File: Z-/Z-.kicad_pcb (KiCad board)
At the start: 4 copper layers, 98 x 98 mm, 144 parts, among them J1 200528-0100, J2 U.FL, J3 U.FL, J4 200528-0100, J5 Conn_01x02, K1 IM02DGR, Q1 NX3008NBKS, Q10 NX3008NBKS, Q11 IRLML2803, Q12 MBT2222ADW1T1, Q13 IRLML2803, Q14 NX3008NBKS, Q15 IRF7404, Q16 MBT2222ADW1T1, Q17 IRF7404, Q18 IRLML2803, Q19 IRF7404, Q2 NX3008NBKS, Q3 MBT2222ADW1T1, Q4 MBT2222ADW1T1, Q5 NX3008NBKS, Q6 NX3008NBKS, Q7 MBT2222ADW1T1, Q8 MBT2222ADW1T1, Q9 MMBT2222AT, U1 OPT4003DNPRQ1, U2 LTC4316xDD, U3 ADM1176-1ARMZ-R7, U4 NCV891330PD50R2G, U5 DRV8830DRC

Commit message: Z- Solar Panel files upload
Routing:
- net VDRIVE: track 32.0 -> 30.6 mm
- net SDA: track 97.2 -> 96.6 mm
- net SCL: track 90.8 -> 90.2 mm
- net Net-(D1-A): track 7.13 -> 6.58 mm

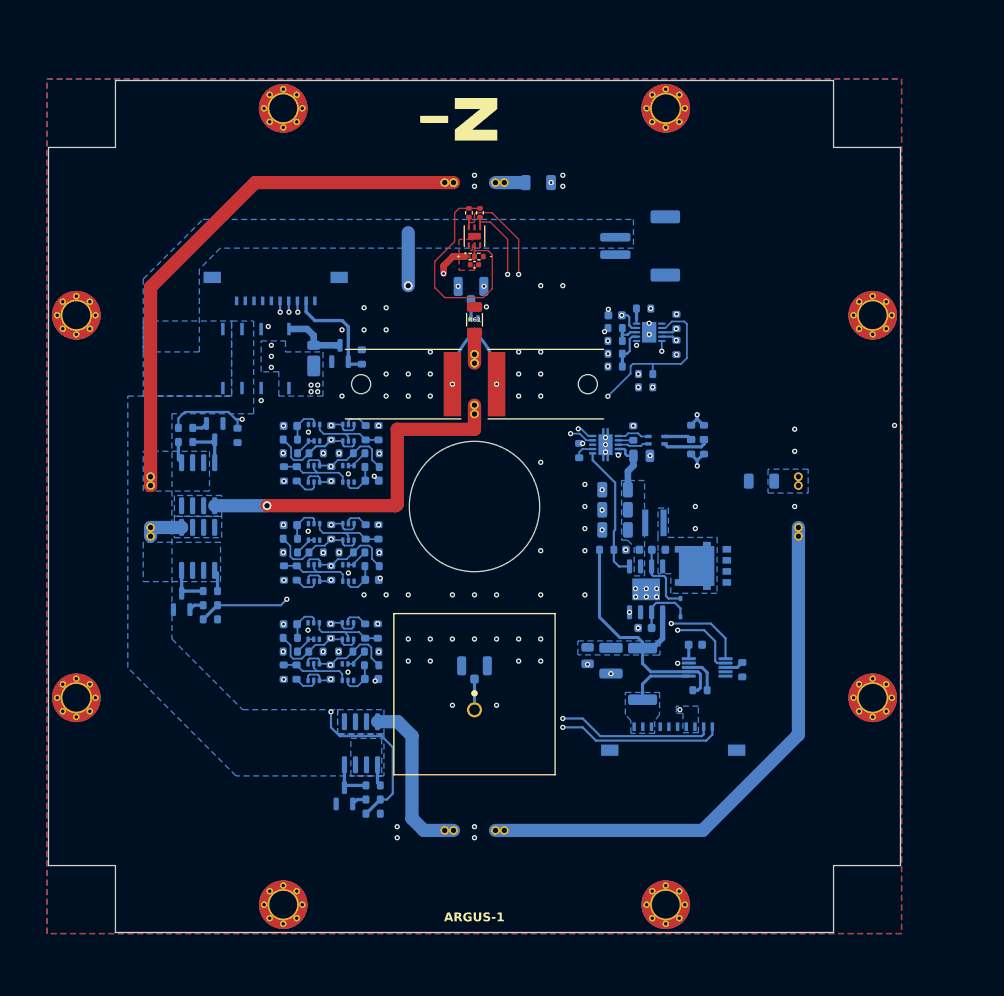
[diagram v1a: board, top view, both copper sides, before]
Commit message: Added i2c expander for burnwires, reformatted i2c protection, swapped to drv8235
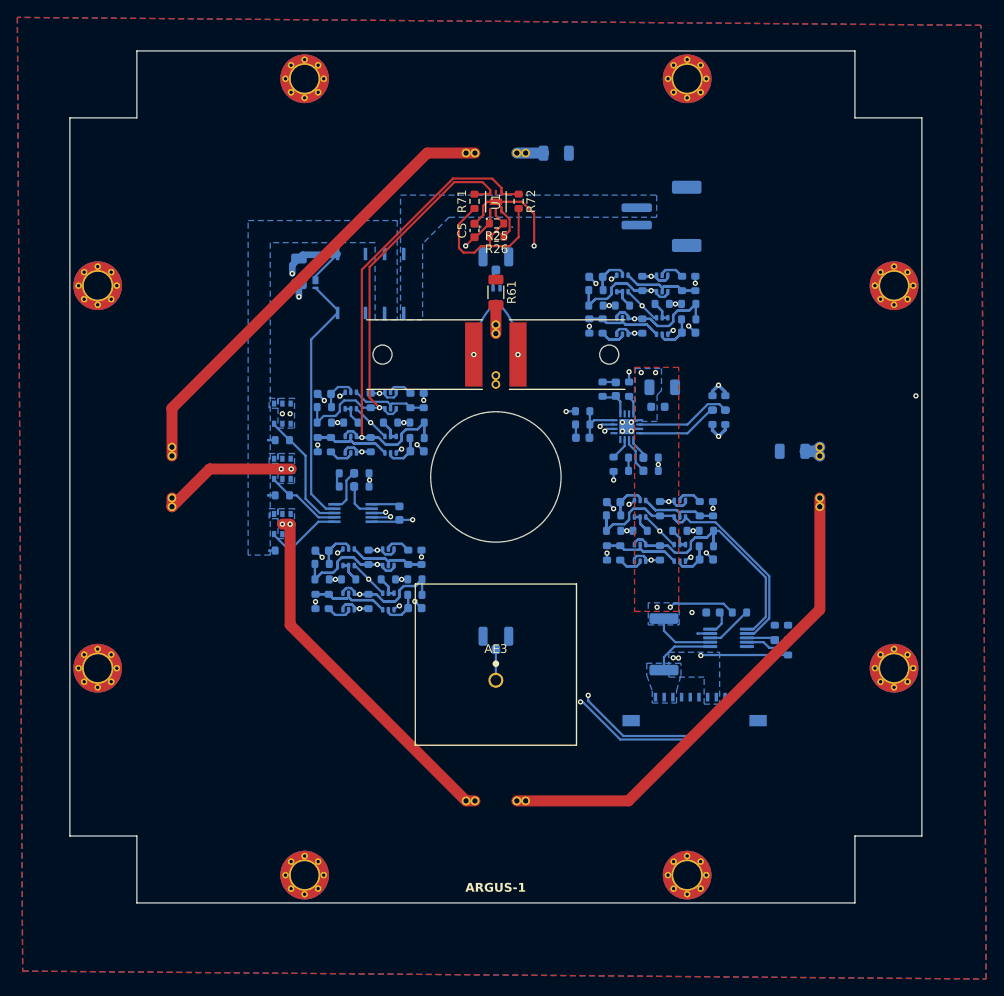
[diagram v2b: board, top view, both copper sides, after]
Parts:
- removed C17: 0.1uF, Capacitor_SMD:C_0603_1608Metric
- removed C18: 10nF, Capacitor_SMD:C_0603_1608Metric
- removed D2: NRVB440MFS, SolarPanels:NRVB440MFSWFT1G
- removed D3: DFLS130L, Diode_SMD:D_PowerDI-123
- removed FL1: SRF2012, SolarPanels:SRF2012
- removed G***: LOGO, LOGO
- removed J4: 200528-0100, Connector_FFC-FPC:Molex_200528-0100_1x10-1MP_P1.00mm_Horizontal
- removed L1: XGL3520-222, SolarPanels:XGL3520
- removed R15, R16, R35, R36, R47, R48: DNI (0R), Resistor_SMD:R_0603_1608Metric
- removed Ref**: Val**, custom-footprints:ypanel
- removed U5: DRV8830DRC, Package_SON:VSON-10-1EP_3x3mm_P0.5mm_EP1.65x2.4mm
- added R73: 10K, Resistor_SMD:R_0603_1608Metric, B.Cu at (175.3, 73.4)
- added R74: 10K, Resistor_SMD:R_0603_1608Metric, B.Cu at (163.8, 75.9)
- added R75: 200K, Resistor_SMD:R_0603_1608Metric, B.Cu at (163.8, 74.2)
- added R76: 680R, Resistor_SMD:R_0603_1608Metric, B.Cu at (166.6, 104.4)
- added R77: 100K, Resistor_SMD:R_0603_1608Metric, B.Cu at (173.5, 101.9)
- added R78: DNI (0R), Resistor_SMD:R_0603_1608Metric, B.Cu at (171.2, 104.4)
- added R79: 10K, Resistor_SMD:R_0603_1608Metric, B.Cu at (165.1, 104.4)
- added R82: 10K, Resistor_SMD:R_0603_1608Metric, B.Cu at (176.5, 101.9)
- added R83: 200K, Resistor_SMD:R_0603_1608Metric, B.Cu at (176.5, 103.6)
- added R84: 680R, Resistor_SMD:R_0603_1608Metric, B.Cu at (175.8, 99.3)
- added R85: 100K, Resistor_SMD:R_0603_1608Metric, B.Cu at (168.9, 101.9)
- added R86: DNI (0R), Resistor_SMD:R_0603_1608Metric, B.Cu at (171.2, 99.3)
- added R87: 10K, Resistor_SMD:R_0603_1608Metric, B.Cu at (177.3, 99.3)
- added R88: 10K, Resistor_SMD:R_0603_1608Metric, B.Cu at (165.9, 101.9)
- added R89: 200K, Resistor_SMD:R_0603_1608Metric, B.Cu at (165.9, 100.1)
- C10: value 0.1uF -> 10uF; footprint Capacitor_SMD:C_0603_1608Metric -> Capacitor_SMD:C_1206_3216Metric
- C11, C12: value 0.1uF -> 10nF
- C13: value 10uF -> 0.1uF; footprint Capacitor_SMD:C_1206_3216Metric -> Capacitor_SMD:C_0603_1608Metric
- C14, C15: value 10uF -> 10nF; footprint Capacitor_SMD:C_1206_3216Metric -> Capacitor_SMD:C_0603_1608Metric
- C16: value 10nF -> 10uF; footprint Capacitor_SMD:C_0603_1608Metric -> Capacitor_SMD:C_1206_3216Metric
- C5: footprint Capacitor_SMD:C_0402_1005Metric -> Capacitor_SMD:C_0603_1608Metric
- C7: value 4.7uF -> 0.1uF; footprint Capacitor_SMD:C_1210_3225Metric -> Capacitor_SMD:C_0603_1608Metric
- C8: value 0.1uF -> 1nF; footprint Capacitor_SMD:C_0805_2012Metric -> Capacitor_SMD:C_0603_1608Metric
- C9: value 1uF -> 0.1uF; footprint Capacitor_SMD:C_0805_2012Metric -> Capacitor_SMD:C_0603_1608Metric
- D1: value BAS16HT1G -> PTVS5V0Z1USK; footprint Diode_SMD:D_SOD-323 -> Diode_SMD:Nexperia_DSN1608-2_1.6x0.8mm
- K1: value IM02DGR -> IM11DGR
- Q10, Q14, Q2, Q6: value NX3008NBKS -> MBT2222ADW1T1
- Q11, Q13: value IRLML2803 -> NX3008NBKS; footprint Package_TO_SOT_SMD:SOT-23 -> Package_TO_SOT_SMD:SOT-363_SC-70-6
- Q15, Q17, Q19: value IRF7404 -> IRFTS9342PBF; footprint Package_SO:SOIC-8_3.9x4.9mm_P1.27mm -> Package_SO:TSOP-6_1.65x3.05mm_P0.95mm
- Q16, Q3, Q7: value MBT2222ADW1T1 -> NX3008NBKS
- Q18: value IRLML2803 -> MBT2222ADW1T1; footprint Package_TO_SOT_SMD:SOT-23 -> Package_TO_SOT_SMD:SOT-363_SC-70-6
- Q9: value MMBT2222AT -> NX3008NBKS; footprint Package_TO_SOT_SMD:SOT-23 -> Package_TO_SOT_SMD:SOT-363_SC-70-6
- R12, R37, R39, R49, R56, R62: value 10K -> 0R
- R14, R40: value 100K -> 10K
- R18, R45: value 10K -> 200K
- R19, R33: value 10K -> 680R
- R20, R34: value 200K -> 100K
- R21, R29: value 10K -> DNI (0R)
- R22: value 200K -> 10K
- R23: value 680R -> 10K
- R24: value 680R -> 200K
- R25, R26, R71, R72: footprint Resistor_SMD:R_0402_1005Metric -> Resistor_SMD:R_0603_1608Metric
- R27: value 100K -> 680R
- R3, R50: value 680R -> 100K
- R38: value 680R -> DNI (0R)
- R41, R51, R59: value 4.7K -> 0R
- R46: value 200K -> 680R
- R5, R52: value 100K -> DNI (0R)
- R63: value 10K -> 10k
- R64: value 10K -> TBD
- R65: value ? -> TBD
- R66: value ? -> 560R
- R67: value ? -> 0R
- R68: value ? -> 680R
- R69: value 0R (DNI) -> 100K
- R70: value 0R (DNI) -> DNI (0R)
- U2: value LTC4316xDD -> PCA9633DP2; footprint Package_DFN_QFN:DFN-10-1EP_3x3mm_P0.5mm_EP1.65x2.38mm -> SolarPanels:SOT552-1_NXP
- U4: value NCV891330PD50R2G -> DRV8235RTER; footprint Package_SO:SOIC-8-1EP_3.9x4.9mm_P1.27mm_EP2.514x3.2mm -> SolarPanels:WQFN16_RTE_TEX
- moved R59 73.8 mm to (185.9, 115.3), turned to -90 degrees
- moved R56 65.8 mm to (184.4, 113.5)
- moved Q11 62.5 mm to (166.9, 73.4)
- moved Q12 60.0 mm to (171.4, 73.4), turned to -90 degrees
- moved R58 58.7 mm to (174.5, 77.5), turned to 180 degrees
- moved R57 58.6 mm to (174.5, 75.8), turned to 0 degrees
- moved D1 56.2 mm to (131.6, 73.3)
- moved R52 55.2 mm to (169.2, 78.3), turned to -90 degrees
- moved Q18 54.2 mm to (173.5, 99.3)
- moved R39 53.5 mm to (170.2, 95.0)
- moved R49 52.0 mm to (170.2, 93.4)
- moved R41 51.3 mm to (168.4, 95.0)
- moved R50 50.8 mm to (171.4, 75.8), turned to 180 degrees
- moved Q10 50.8 mm to (166.9, 78.3), turned to 90 degrees
- moved R51 49.6 mm to (168.4, 93.4)
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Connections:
- C10 pad 1: GND -> VDRIVE
- C10 pad 2: Net-(D1-A) -> GND
- C11 pad 1: Net-(D1-K) -> Net-(Q9B-G1)
- C11 pad 2: /I2C Devices/SW -> GND
- C12 pad 1: GND -> Net-(Q11B-G1)
- C12 pad 2: +5V -> GND
- C13 pad 1: GND -> 3.3V
- C13 pad 2: +5V -> GND
- C14 pad 1: GND -> Net-(Q13B-G1)
- C14 pad 2: +5V -> GND
- C15 pad 1: GND -> Net-(Q16B-G1)
- C15 pad 2: +5V -> GND
- C16 pad 1: Net-(Q10B-G1) -> 3.3V
- C2 pad 1: Net-(Q2B-G1) -> Net-(Q3B-G1)
- C4 pad 1: Net-(Q6B-G1) -> Net-(Q7B-G1)
- C7 pad 1: GND -> /I2C Devices/VREF
- C7 pad 2: VDRIVE -> GND
- C8 pad 1: +5V -> /I2C Devices/IPROPI
- C9 pad 1: GND -> VDRIVE
- C9 pad 2: VDRIVE -> GND
- D1 pad 1: Net-(D1-K) -> 3.3V
- D1 pad 2: Net-(D1-A) -> BURN_RELAY_A
- K1 pad 1: VBATT -> 3.3V
- K1 pad 8: Net-(D3-A) -> BURN_RELAY_A
- Q10 pad 1: GND -> SCL
- Q10 pad 2: Net-(Q10A-G2) -> Net-(Q10A-B1)
- Q10 pad 3: Net-(Q10A-G2) -> SCL
- Q10 pad 4: GND -> SCL_M
- Q10 pad 5: Net-(Q10B-G1) -> Net-(Q10B-B2)
- Q10 pad 6: Net-(Q10A-D1) -> SCL_M
- Q11 pad 1: Net-(Q11-G) -> GND
- Q11 pad 2: GND -> Net-(Q11A-G2)
- Q11 pad 3: Net-(Q11-D) -> Net-(Q11A-G2)
- Q12 pad 1: SCL -> SDA
- Q12 pad 3: SCL -> SDA
- Q12 pad 4: SCL_CPWR -> SDA_M
- Q12 pad 5: Net-(Q10A-D1) -> Net-(Q11A-D1)
- Q12 pad 6: SCL_CPWR -> SDA_M
- Q13 pad 1: Net-(Q13-G) -> GND
- Q13 pad 2: GND -> Net-(Q13A-G2)
- Q13 pad 3: Net-(Q13-D) -> Net-(Q13A-G2)
- Q14 pad 1: GND -> SCL
- Q14 pad 2: Net-(Q14A-G2) -> Net-(Q14A-B1)
- Q14 pad 3: Net-(Q14A-G2) -> SCL
- Q14 pad 4: GND -> SCL_CPWR
- Q14 pad 5: Net-(Q14B-G1) -> Net-(Q13A-D1)
- Q14 pad 6: Net-(Q14A-D1) -> SCL_CPWR
- Q15 pad 1: /Burn Wires/VBURN_A_IN -> /Burn Wires/VBURN1
- Q15 pad 2: /Burn Wires/VBURN_A_IN -> /Burn Wires/VBURN1
- Q15 pad 3: /Burn Wires/VBURN_A_IN -> BURN_EN1
- Q15 pad 4: Net-(Q11-D) -> /Burn Wires/VBURN_A_IN
- Q16 pad 1: SDA -> GND
- Q16 pad 2: Net-(Q16A-B1) -> Net-(Q16A-G2)
- Q16 pad 3: SDA -> Net-(Q16A-G2)
- Q16 pad 4: SDA_CPWR -> GND
- Q16 pad 5: Net-(Q14A-D1) -> Net-(Q16B-G1)
- Q16 pad 6: SDA_CPWR -> Net-(Q16A-D1)
- Q17 pad 1: /Burn Wires/VBURN_A_IN -> /Burn Wires/VBURN2
- Q17 pad 2: /Burn Wires/VBURN_A_IN -> /Burn Wires/VBURN2
- Q17 pad 3: /Burn Wires/VBURN_A_IN -> BURN_EN2
- Q17 pad 4: Net-(Q13-D) -> /Burn Wires/VBURN_A_IN
- Q18 pad 1: Net-(Q18-G) -> SDA
- Q18 pad 2: GND -> Net-(Q18A-B1)
- Q18 pad 3: Net-(Q18-D) -> SDA
- Q19 pad 1: /Burn Wires/VBURN_A_IN -> /Burn Wires/VBURN3
- Q19 pad 2: /Burn Wires/VBURN_A_IN -> /Burn Wires/VBURN3
- Q19 pad 3: /Burn Wires/VBURN_A_IN -> BURN_EN3
- Q19 pad 4: Net-(Q18-D) -> /Burn Wires/VBURN_A_IN
- Q2 pad 1: GND -> SCL
- Q2 pad 2: Net-(Q2A-G2) -> Net-(Q2A-B1)
- Q2 pad 3: Net-(Q2A-G2) -> SCL
- Q2 pad 4: GND -> SCL_LS
- Q2 pad 5: Net-(Q2B-G1) -> Net-(Q1A-D1)
- Q2 pad 6: Net-(Q2A-D1) -> SCL_LS
- Q3 pad 1: SCL -> GND
- Q3 pad 2: Net-(Q3A-B1) -> Net-(Q3A-G2)
- Q3 pad 3: SCL -> Net-(Q3A-G2)
- Q3 pad 4: SCL_LS -> GND
- Q3 pad 5: Net-(Q1A-D1) -> Net-(Q3B-G1)
- Q3 pad 6: SCL_LS -> Net-(Q3A-D1)
- Q4 pad 1: SCL -> SDA
- Q4 pad 3: SCL -> SDA
- Q4 pad 4: SCL_M -> SDA_LS
- Q4 pad 5: Net-(Q2A-D1) -> Net-(Q3A-D1)
- Q4 pad 6: SCL_M -> SDA_LS
- Q6 pad 1: GND -> SCL
- Q6 pad 2: Net-(Q6A-G2) -> Net-(Q6A-B1)
- Q6 pad 3: Net-(Q6A-G2) -> SCL
- Q6 pad 4: GND -> SCL_IO
- Q6 pad 5: Net-(Q6B-G1) -> Net-(Q5A-D1)
- Q6 pad 6: Net-(Q6A-D1) -> SCL_IO
- Q7 pad 1: SDA -> GND
- Q7 pad 2: Net-(Q7A-B1) -> Net-(Q7A-G2)
- Q7 pad 3: SDA -> Net-(Q7A-G2)
- Q7 pad 4: SDA_LS -> GND
- Q7 pad 5: Net-(Q5A-D1) -> Net-(Q7B-G1)
- Q7 pad 6: SDA_LS -> Net-(Q7A-D1)
- Q8 pad 4: SDA_M -> SDA_IO
- Q8 pad 5: Net-(Q6A-D1) -> Net-(Q7A-D1)
- Q8 pad 6: SDA_M -> SDA_IO
- Q9 pad 1: BURN_RELAY_A -> GND
- Q9 pad 2: GND -> Net-(Q9A-G2)
- Q9 pad 3: Net-(D3-A) -> Net-(Q9A-G2)
- R1 pad 1: Net-(Q3A-B1) -> Net-(Q2A-B1)
- R10 pad 1: GND -> /I2C Devices/A0_CPWR
- R10 pad 2: Net-(U3-A0) -> 3.3V
- R11 pad 1: GND -> /I2C Devices/A0_IO
- R11 pad 2: Net-(U5-A0) -> 3.3V
- R12 pad 1: M_FAULT -> GND
- R12 pad 2: VDRIVE -> /I2C Devices/A0_IO
- R13 pad 1: GND -> /I2C Devices/A1_IO
- R13 pad 2: Net-(U5-ISENSE) -> 3.3V
- R14 pad 2: Net-(Q2A-G2) -> Net-(Q1A-D1)
- R17 pad 2: Net-(Q1A-D1) -> SCL_LS
- R18 pad 1: 3.3V -> SCL_LS
- R18 pad 2: Net-(Q2A-D1) -> Net-(Q1B-G1)
- R19 pad 1: 3.3V -> Net-(Q4A-B1)
- R19 pad 2: SCL_LS -> Net-(Q3A-D1)
- R20 pad 1: SCL_LS -> 3.3V
- R20 pad 2: Net-(Q1B-G1) -> Net-(Q3A-G2)
- R21 pad 1: 3.3V -> SDA_LS
- R21 pad 2: SCL_M -> SDA
- R22 pad 1: SCL_M -> 3.3V
- R22 pad 2: Net-(Q2B-G1) -> Net-(Q3A-D1)
- R23 pad 1: Net-(Q7A-B1) -> 3.3V
- R23 pad 2: Net-(Q5A-D1) -> SDA_LS
- R24 pad 1: Net-(Q8A-B1) -> SDA_LS
- R24 pad 2: Net-(Q6A-D1) -> Net-(Q3B-G1)
- R27 pad 1: 3.3V -> Net-(Q6A-B1)
- R27 pad 2: Net-(Q5A-G2) -> Net-(Q5A-D1)
- R28 pad 2: Net-(Q6A-G2) -> Net-(Q5A-G2)
- R29 pad 1: 3.3V -> SCL_IO
- R29 pad 2: Net-(Q5A-D1) -> SCL
- R3 pad 1: Net-(Q4A-B1) -> 3.3V
- R3 pad 2: Net-(Q2A-D1) -> Net-(Q1A-G2)
- R30 pad 2: Net-(Q6A-D1) -> Net-(Q5A-D1)
- R31 pad 2: SDA_LS -> SCL_IO
- R32 pad 1: SDA_LS -> SCL_IO
- R33 pad 1: 3.3V -> Net-(Q8A-B1)
- R33 pad 2: SDA_M -> Net-(Q7A-D1)
- R34 pad 1: SDA_M -> 3.3V
- R34 pad 2: Net-(Q6B-G1) -> Net-(Q7A-G2)
- R37 pad 1: BURN_RELAY_A -> GND
- R37 pad 2: GND -> /I2C Devices/A1_IO
- R38 pad 1: Net-(Q12A-B1) -> SDA_IO
- R38 pad 2: Net-(Q10A-D1) -> SDA
- R39 pad 1: BURN_EN1 -> /I2C Devices/A0_COIL
- R39 pad 2: GND -> 3.3V
- R40 pad 2: Net-(Q10A-G2) -> Net-(Q7A-D1)
- R41 pad 1: Net-(Q11-G) -> GND
- R41 pad 2: BURN_EN1 -> /I2C Devices/A0_COIL
- R42 pad 2: Net-(Q10A-D1) -> SDA_IO
- R43 pad 1: Net-(Q11-D) -> BURN_EN1
- R45 pad 1: 3.3V -> SDA_IO
- R45 pad 2: SCL_CPWR -> Net-(Q7B-G1)
- R46 pad 1: SCL_CPWR -> Net-(Q10A-B1)
- R46 pad 2: Net-(Q10B-G1) -> Net-(Q10B-B2)
- R49 pad 1: BURN_EN2 -> /I2C Devices/A1_COIL
- R49 pad 2: GND -> 3.3V
- R5 pad 1: 3.3V -> SCL_LS
- R5 pad 2: Net-(Q1A-G2) -> SCL
- R50 pad 1: Net-(Q16A-B1) -> 3.3V
- R50 pad 2: Net-(Q14A-D1) -> Net-(Q9A-G2)
- R51 pad 1: Net-(Q13-G) -> GND
- R51 pad 2: BURN_EN2 -> /I2C Devices/A1_COIL
- R52 pad 1: 3.3V -> SCL_M
- R52 pad 2: Net-(Q14A-G2) -> SCL
- R53 pad 1: Net-(Q13-D) -> BURN_EN2
- R54 pad 2: Net-(Q14A-D1) -> Net-(Q10B-B2)
- R56 pad 1: BURN_EN3 -> GND
- R56 pad 2: GND -> /I2C Devices/A0_CPWR
- R57 pad 2: SDA_CPWR -> SCL_M
- R58 pad 1: SDA_CPWR -> SCL_M
- R58 pad 2: Net-(Q14B-G1) -> Net-(Q9B-G1)
- R59 pad 1: Net-(Q18-G) -> /I2C Devices/A1_CPWR
- R59 pad 2: BURN_EN3 -> 3.3V
- R60 pad 1: Net-(Q18-D) -> BURN_EN3
- R62 pad 1: Net-(U2-ENABLE) -> GND
- R62 pad 2: 3.3V -> /I2C Devices/A1_CPWR
- R63 pad 1: /I2C Devices/SDAOUT -> 3.3V
- R63 pad 2: 3.3V -> Net-(U4-NFAULT)
- R64 pad 1: /I2C Devices/SCLOUT -> 3.3V
- R64 pad 2: 3.3V -> /I2C Devices/VREF
- R65 pad 1: GND -> /I2C Devices/VREF
- R65 pad 2: Net-(U2-XORL) -> GND
- R66 pad 1: Net-(U2-XORL) -> /I2C Devices/IPROPI
- R66 pad 2: 3.3V -> GND
- R67 pad 1: GND -> Net-(U4-NSLEEP)
- R67 pad 2: Net-(U2-XORH) -> 3.3V
- R68 pad 1: Net-(U2-XORH) -> Net-(Q12A-B1)
- R68 pad 2: 3.3V -> Net-(Q11A-D1)
- R69 pad 1: SCL_LS -> 3.3V
- R69 pad 2: /I2C Devices/SCLOUT -> Net-(Q11A-G2)
- R70 pad 1: SDA_LS -> SDA_M
- R70 pad 2: /I2C Devices/SDAOUT -> SDA
- R71 pad 2: /I2C Devices/SDAOUT -> SDA_LS
- R72 pad 1: /I2C Devices/SCLOUT -> SCL_LS
- U1 pad 4: /I2C Devices/SCLOUT -> SCL_LS
- U1 pad 6: /I2C Devices/SDAOUT -> SDA_LS
- U2 pad 1: GND -> BURN_EN2
- U2 pad 10: SCL_LS -> 3.3V
- U2 pad 2: Net-(U2-XORH) -> BURN_EN1
- U2 pad 3: Net-(U2-XORL) -> BURN_EN3
- U2 pad 4: 3.3V -> BURN_RELAY_A
- U2 pad 5: Net-(U2-ENABLE) -> /I2C Devices/A0_IO
- U2 pad 6: unconnected-(U2-READY-Pad6) -> GND
- U2 pad 7: SDA_LS -> /I2C Devices/A1_IO
- U2 pad 8: /I2C Devices/SDAOUT -> SCL_IO
- U2 pad 9: /I2C Devices/SCLOUT -> SDA_IO
- U3 pad 8: Net-(U3-A0) -> /I2C Devices/A0_CPWR
- U3 pad 9: GND -> /I2C Devices/A1_CPWR
- U4 pad 1: VDRIVE -> /I2C Devices/IPROPI
- U4 pad 2: Net-(D1-A) -> unconnected-(U4-RSVD-Pad2)
- U4 pad 4: GND -> Net-(U4-NFAULT)
- U4 pad 5: M_FAULT -> VDRIVE
- U4 pad 6: +5V -> COIL_P
- U4 pad 7: Net-(D1-K) -> GND
- U4 pad 8: /I2C Devices/SW -> COIL_N
- U4 pad 9: GND -> /I2C Devices/A1_COIL
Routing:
- net GND: track 0.00 -> 65.1 mm, vias 107 -> 27
- net SDA: track 96.6 -> 161.1 mm, vias 4 -> 5
- net SCL: track 90.2 -> 154.7 mm, vias 4 -> 5
- net BURN_EN2: track 71.3 -> 9.15 mm, vias 2 -> 0
- net 3.3V: track 113.9 -> 64.6 mm, vias 26 -> 27
- net /I2C Devices/SDAOUT: track 47.3 -> 0.00 mm, vias 3 -> 0
- net /I2C Devices/SCLOUT: track 42.9 -> 0.00 mm, vias 3 -> 0
- net SCL_IO: track 0.00 -> 39.4 mm, vias 0 -> 2
- net BURN_EN1: track 45.4 -> 8.83 mm, vias 2 -> 0
- net SDA_IO: track 0.00 -> 35.4 mm, vias 0 -> 2
- net VBATT: track 27.7 -> 0.00 mm, vias 8 -> 0
- net /Burn Wires/VBURN2: track 19.5 -> 42.1 mm, vias 0 -> 2
- net SCL_CPWR: track 62.7 -> 42.6 mm, vias 2 -> 0
- net Net-(Q10B-B2): track 0.00 -> 19.5 mm
- net Net-(Q11A-D1): track 0.00 -> 18.1 mm
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- added copper zone on F.Cu, net VDRIVE
- removed copper zone on B.Cu, net +5V
- removed copper zone on B.Cu, net /I2C Devices/SW
- removed copper zone on F.Cu, net 3.3V
- removed copper zone on In1.Cu, net GND
- removed copper zone on B.Cu, net Net-(JP5-Pad2)
- removed copper zone on In1.Cu, net VBATT
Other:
- board text added: "ARGUS-1 Cubesat Carnegie Mellon University Z- Solar Panel v2"
- board text removed: "ALUN"
- board text removed: "ARGUS-1 Cubesat Carnegie Mellon University Z- Solar Panel v1"
- board text removed: "BURN WIRE 1"
- board text removed: "BURN WIRE 2"
- board text removed: "BURN WIRE 3"
- board text removed: "BURNWIRE 1"
- board text removed: "BURNWIRE 2"
- board text removed: "BURNWIRE 3"
- board text removed: "BURN_EN1"
- board text removed: "BURN_EN2"
- board text removed: "BURN_EN3"
- board text removed: "BURN_EN4"
- board text removed: "COIL DRIVER"
- board text removed: "COIL PWR MONITOR"
- board text removed: "GPS ANT"
- board text removed: "I2C ADDR TRANSLATOR"
- board text removed: "I2C BUS PROTECTION"
- board text removed: "MAINBOARD"
- board text removed: "POWER RELAY A"
- board text removed: "REGULATOR BUCK 5V"
- board text removed: "RELAY_A"
- board text removed: "UHF ANT"

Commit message: Moved burnwire around and added switch to coil driver
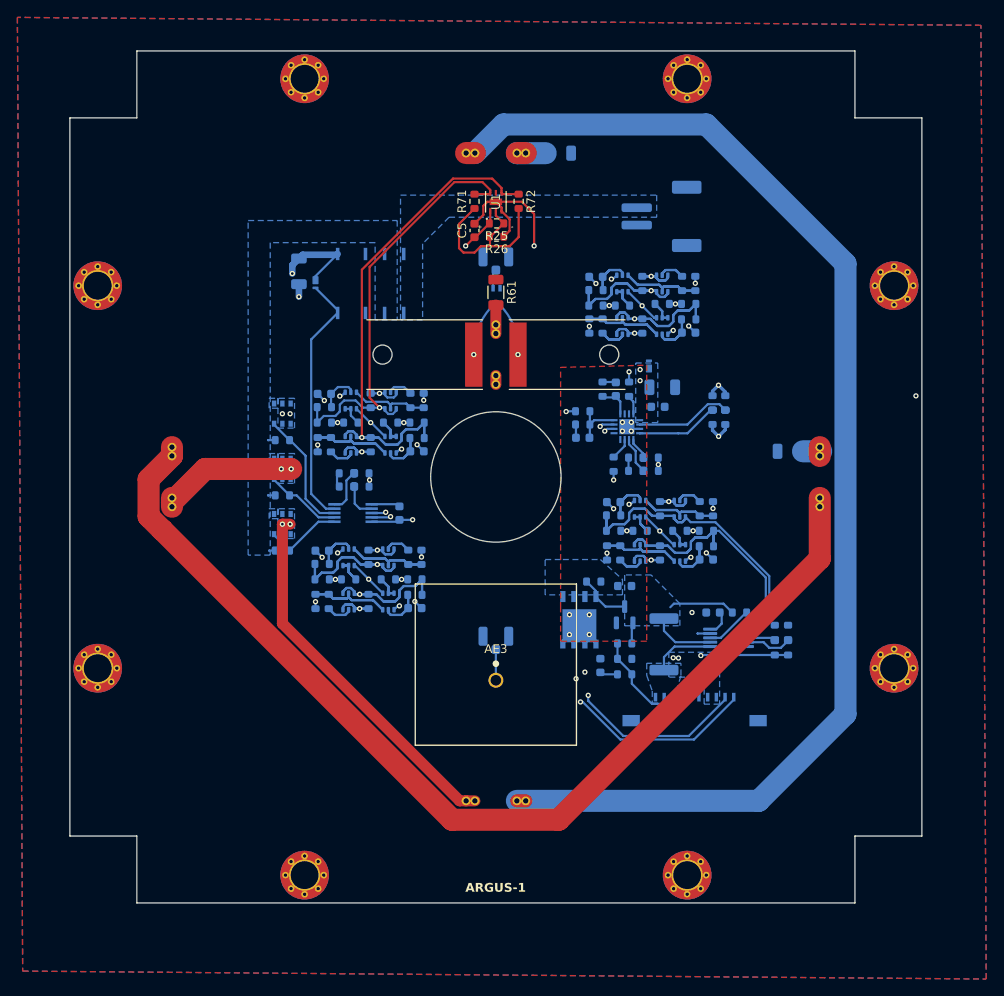
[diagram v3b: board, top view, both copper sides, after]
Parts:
- added D2: GREEN, LED_SMD:LED_0603_1608Metric, B.Cu at (164.3, 117.3)
- added D3: 10V, Diode_SMD:Nexperia_DSN1608-2_1.6x0.8mm, B.Cu at (169.9, 82.9)
- added F1: 500mA, Fuse:Fuse_0603_1608Metric, B.Cu at (167.1, 108.2)
- added Q20: IRLML2803, Package_TO_SOT_SMD:SOT-23, B.Cu at (167.1, 111.5)
- added Q21: SIRA99DP-T1-GE3, Package_SO:PowerPAK_SO-8_Single, B.Cu at (161.9, 112.1)
- added R15: 2.7k, Resistor_SMD:R_0603_1608Metric, B.Cu at (167.1, 118.4)
- added R16: 10k, Resistor_SMD:R_0603_1608Metric, B.Cu at (167.1, 116.6)
- added R35: 4k7, Resistor_SMD:R_0603_1608Metric, B.Cu at (167.1, 114.8)
- added R36: 10k, Resistor_SMD:R_0603_1608Metric, B.Cu at (163.6, 107.7)
- AE1, AE2: footprint SolarPanels:Antenna Mount -> Argus-Miscellaneous:Antenna Mount
- AE3: footprint SolarPanels:ANT_CGGBP.18.4.A.02_TAL -> Argus-Miscellaneous:ANT_CGGBP.18.4.A.02_TAL
- BA1: footprint SolarPanels:ATB2012 -> Argus-Passives:ATB2012
- H1, H2, H3, H4, H5, H6, H7, H8: footprint SolarPanels:MountingHole_3.2mm_M3_DIN965_Pad_TopBottom -> Argus-Miscellaneous:MountingHole_3.2mm_M3_DIN965_Pad_TopBottom
- JP1, JP2, JP3: footprint SolarPanels:Burn-Wire -> Argus-Miscellaneous:Burn-Wire
- JP4: renamed from JP5; footprint SolarPanels:Burn-Wire -> Argus-Miscellaneous:Burn-Wire
- JP5: renamed from JP4; footprint SolarPanels:Burn-Wire -> Argus-Miscellaneous:Burn-Wire
- U1: footprint SolarPanels:OPT4003 -> Argus-IC:OPT4003
- U2: footprint SolarPanels:SOT552-1_NXP -> Argus-IC:SOT552-1_NXP
- U4: footprint SolarPanels:WQFN16_RTE_TEX -> Argus-IC:WQFN16_RTE_TEX
- moved R55 43.6 mm to (159.5, 58.4), turned to 180 degrees
- moved R44 43.6 mm to (186.2, 92.7), turned to 0 degrees
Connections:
- C10 pad 1: VDRIVE -> /I2C Devices/VM
- C9 pad 1: VDRIVE -> /I2C Devices/VM
- J1 pad 7: GND -> COIL_DRIVER_EN
- JP4 pad 1: Net-(JP2-Pad2) -> Net-(JP1-Pad2)
- JP4 pad 2: Net-(JP5-Pad2) -> Net-(JP4-Pad2)
- JP5 pad 1: Net-(JP1-Pad2) -> Net-(JP2-Pad2)
- JP5 pad 2: Net-(JP4-Pad2) -> Net-(JP5-Pad2)
- U4 pad 5: VDRIVE -> /I2C Devices/VM
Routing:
- net Net-(JP2-Pad2): track 56.8 -> 146.4 mm
- net Net-(JP1-Pad2): track 52.5 -> 120.2 mm
- net COIL_DRIVER_EN: track 0.00 -> 12.6 mm
- net Net-(Q20-D): track 0.00 -> 5.98 mm
- net Net-(Q20-G): track 0.00 -> 2.42 mm
- net Net-(D2-A): track 0.00 -> 2.06 mm
- net /Burn Wires/VBURN3: track 27.1 -> 28.1 mm
- net /Burn Wires/VBURN2: track 42.1 -> 42.9 mm
- net Net-(JP5-Pad2): track 3.78 -> 4.34 mm
- net VDRIVE: vias 4 -> 0
- net GND: vias 27 -> 29
- net /I2C Devices/VM: vias 0 -> 6
- added copper zone on B.Cu, net /I2C Devices/VM
- added copper zone on F.Cu, net /I2C Devices/VM
- added copper zone on B.Cu, net Net-(F1-Pad1)
- removed copper zone on F.Cu, net VDRIVE

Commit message: Started adding main/peripheral 3v3 nets
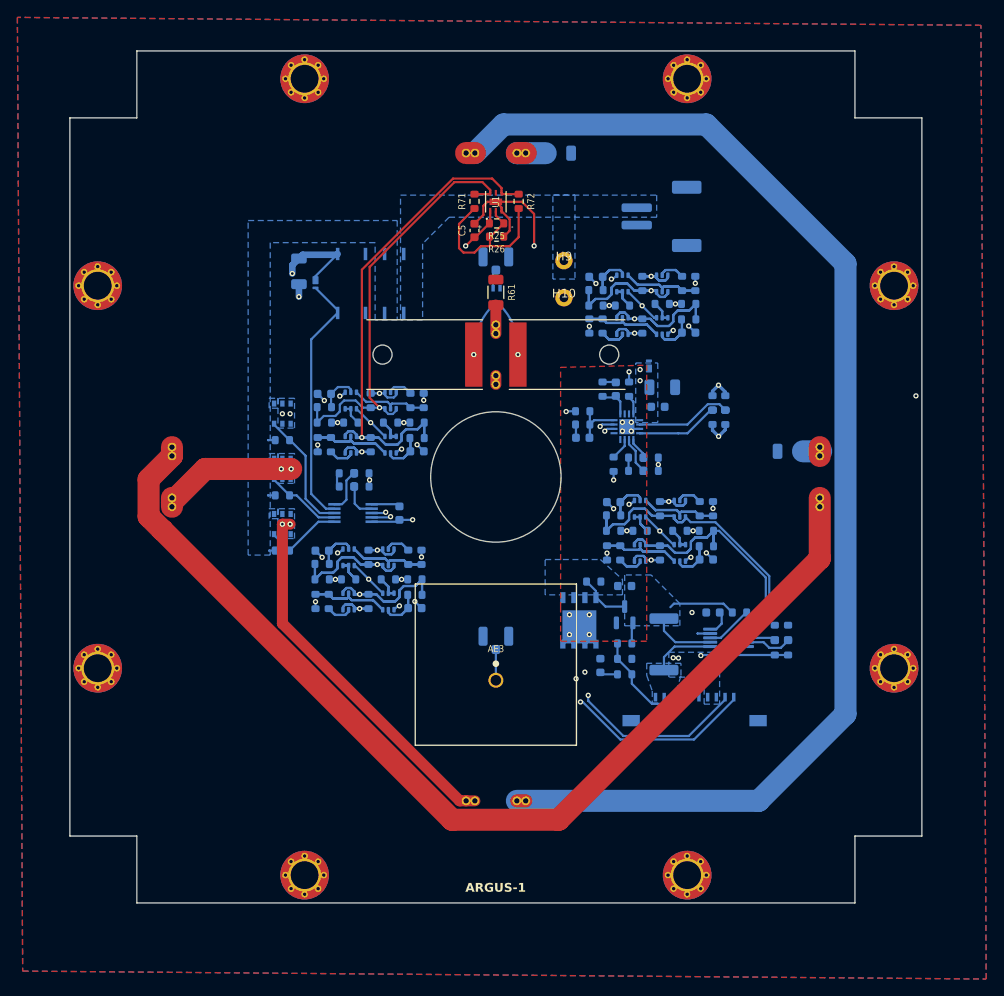
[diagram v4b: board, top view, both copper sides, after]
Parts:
- added H10: MountingHole_Pad, Argus-Connectors:20AWG Through Hole, F.Cu at (160.1, 75.1)
- added H9: MountingHole_Pad, Argus-Connectors:20AWG Through Hole, F.Cu at (160.1, 70.8)
- J1: footprint Connector_FFC-FPC:Molex_200528-0100_1x10-1MP_P1.00mm_Horizontal -> Argus-Connectors:Molex_200528-0100_1x10-1MP_P1.00mm_Horizontal
- K1: footprint SolarPanels:RELAY8_SMTGUL_TEC -> Argus-Miscellaneous:RELAY8_SMTGUL_TEC
- Q21: value SIRA99DP-T1-GE3 -> SiRA99DP; footprint Package_SO:PowerPAK_SO-8_Single -> Argus-Miscellaneous:PowerPAK SO-8
- moved Q21 0.82 mm to (161.9, 112.9), turned to 90 degrees
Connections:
- F1 pad 1: Net-(F1-Pad1) -> Net-(Q21-S)
- Q21 pad 1: Net-(F1-Pad1) -> Net-(Q20-D)
- Q21 pad 2: Net-(F1-Pad1) -> /I2C Devices/VM
- Q21 pad 3: Net-(F1-Pad1) -> Net-(Q21-S)
- R36 pad 2: Net-(F1-Pad1) -> Net-(Q21-S)
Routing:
- added copper zone on B.Cu, net Net-(Q21-S)
- removed copper zone on B.Cu, net Net-(F1-Pad1)
